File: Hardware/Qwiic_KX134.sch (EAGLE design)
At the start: 25 parts, among them J2 QWIIC_RIGHT_ANGLE, J4 QWIIC_RIGHT_ANGLE, U1 KX134

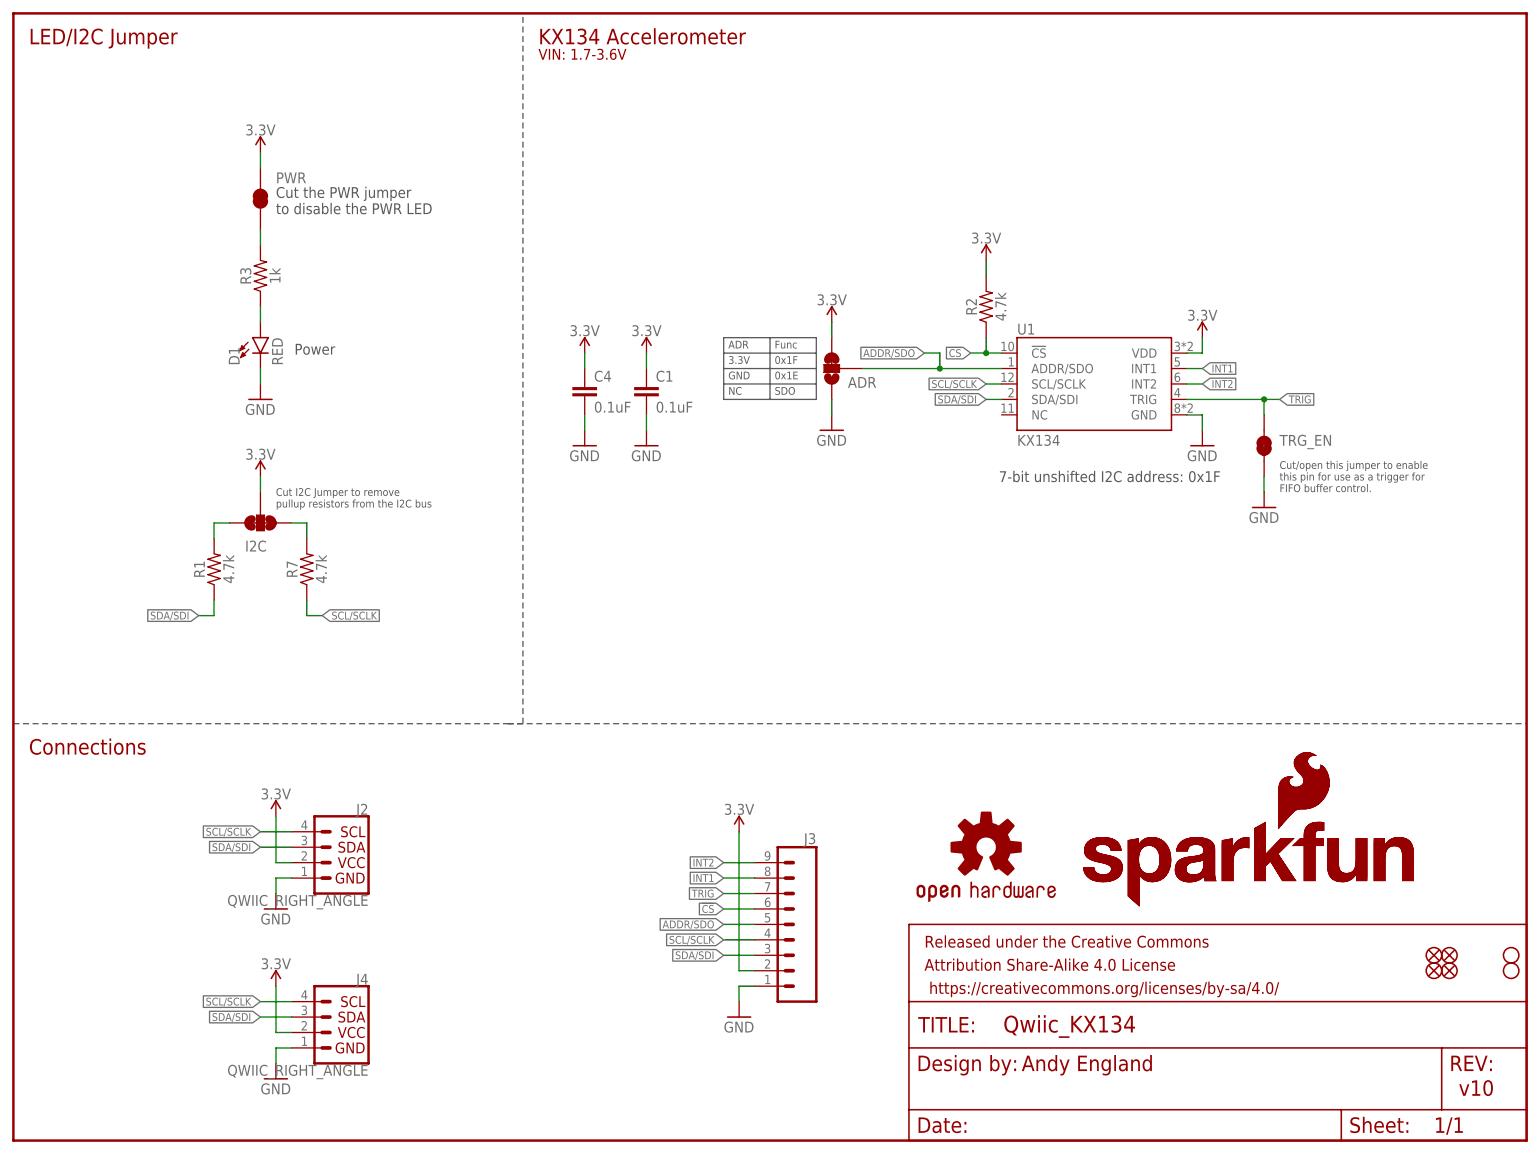
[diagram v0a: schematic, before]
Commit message: Post review/checklist changes
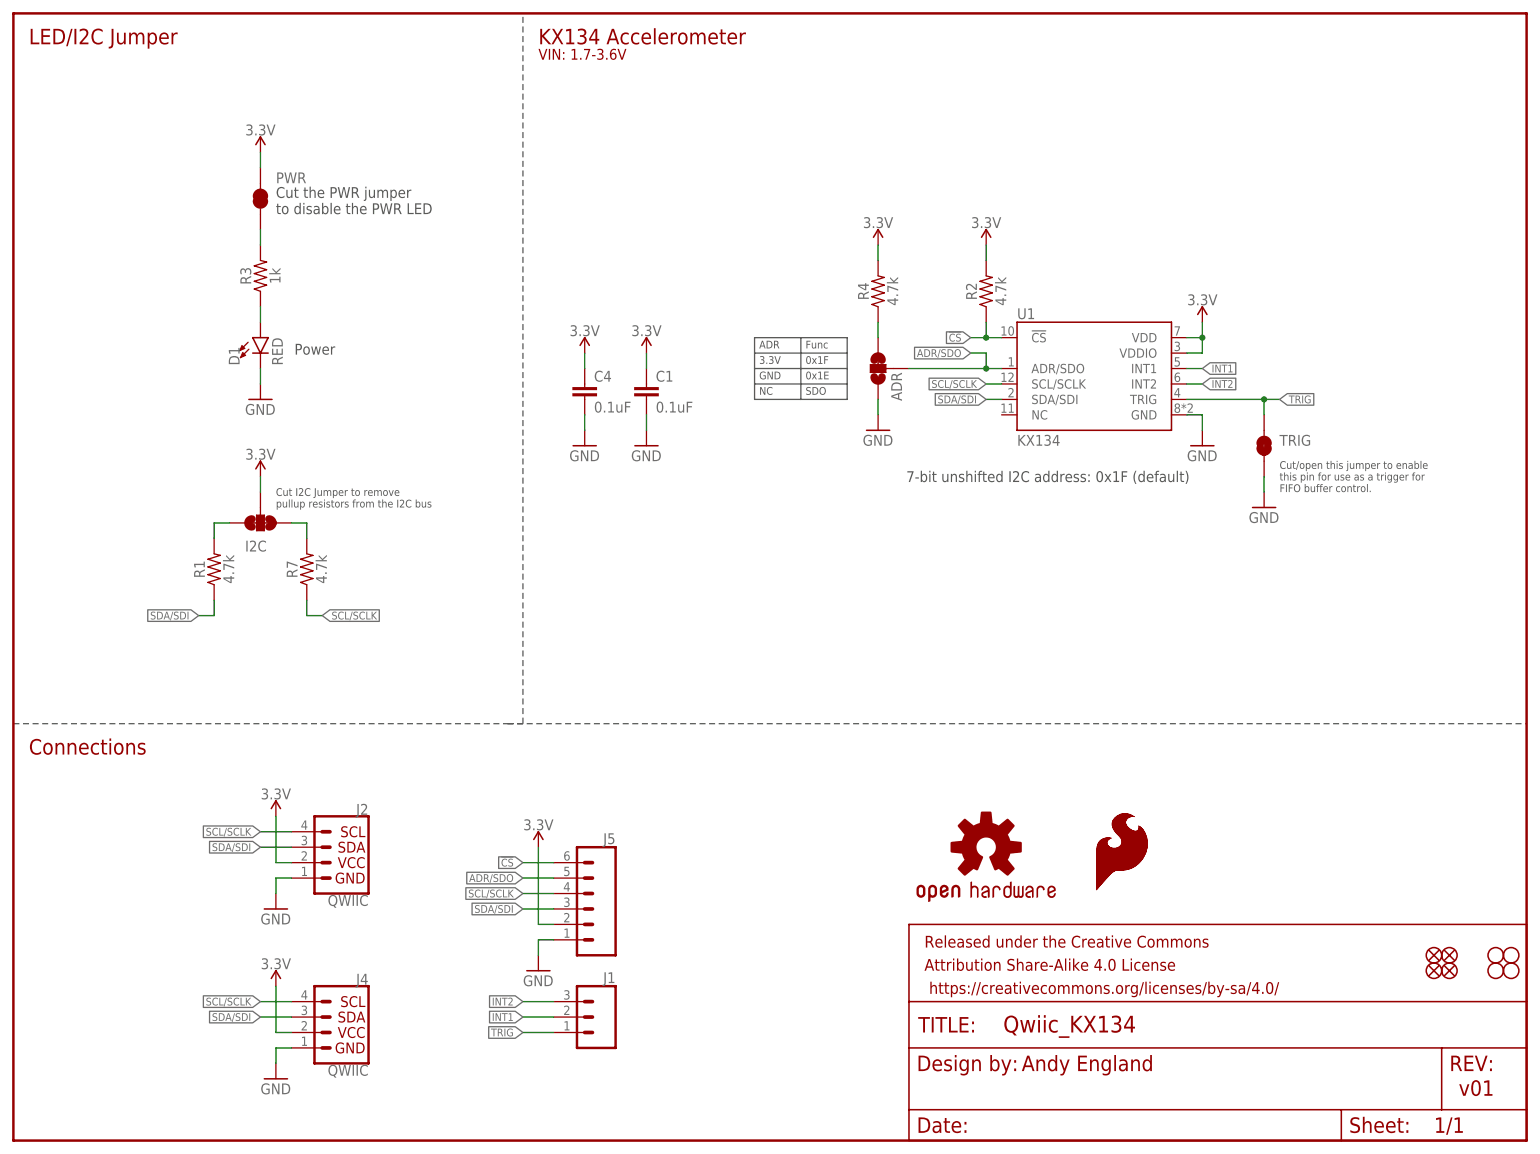
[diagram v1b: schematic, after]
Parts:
- removed J3: (no value), SparkFun-Connectors:CONN_09NO_SILK
- removed LOGO3, LOGO4: SFE_LOGO_NAME_FLAME.1_INCH, SparkFun-Aesthetics:SFE_LOGO_NAME_FLAME.1_INCH
- added J1: (no value), SparkFun-Connectors:CONN_031X03_NO_SILK
- added J5: (no value), SparkFun-Connectors:CONN_06NO_SILK_NO_POP
- added JP7, JP8: STAND-OFF, SparkFun:STAND-OFF
- added LOGO1, LOGO2: SFE_LOGO_FLAME.1_INCH, SparkFun-Aesthetics:SFE_LOGO_FLAME.1_INCH
- added R4: 4.7k, SparkFun-Resistors:4.7KOHM-0603-1/10W-1%
- J2, J4: value QWIIC_RIGHT_ANGLE -> QWIIC
- renumbered TRG_EN to TRIG
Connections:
- removed net ADDR/SDO: ADR.2, J3.5, U1.ADDR/SDO
- new net ADR/SDO: ADR.2, J5.5, U1.ADR/SDO
- new net N$5: ADR.3, R4.1
- net !CS: now also J5.6; no longer J3.6
- net 3.3V: now also J5.2, R4.2, U1.VDDIO; no longer ADR.3, J3.2
- net GND: now also J5.1; no longer J3.1
- net INT1: now also J1.2; no longer J3.8
- net INT2: now also J1.3; no longer J3.9
- net SCL/SCLK: now also J5.4; no longer J3.4
- net SDA/SDI: now also J5.3; no longer J3.3
- net TRIG: now also J1.1; no longer J3.7
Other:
- note added: "7-bit unshifted I2C address: 0x1F (default)"
- note added: "v01"
- note removed: "7-bit unshifted I2C address: 0x1F"
- note removed: "v10"
- moved on the sheet: ADR, R2

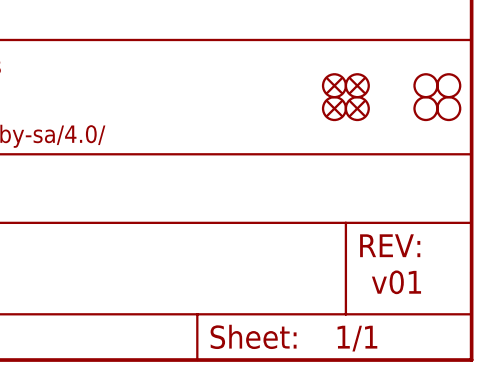
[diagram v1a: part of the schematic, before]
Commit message: updating version number and orientation for review
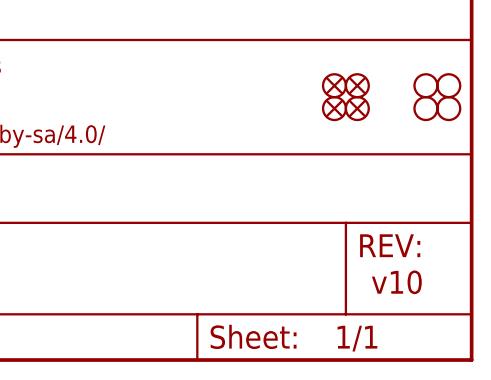
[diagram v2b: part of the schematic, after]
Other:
- note added: "v10"
- note removed: "v01"
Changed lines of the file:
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@@
 <sheet>
 <plain>
-<text x="237.744" y="7.366" size="2.54" layer="94" font="vector">v01</text>
+<text x="237.744" y="7.366" size="2.54" layer="94" font="vector">v10</text>
 <text x="170.18" y="109.22" size="1.778" layer="97" font="vector" align="center">7-bit unshifted I2C address: 0x1F (default)</text>
 <text x="46.228" y="129.286" size="1.778" layer="97" font="vector">Power</text>

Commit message: post design review, computer transfer
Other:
- note removed: "NC"
- note removed: "SDO"
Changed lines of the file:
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@@
 <wire x1="137.16" y1="129.54" x2="137.16" y2="127" width="0.1524" layer="97"/>
 <wire x1="137.16" y1="127" x2="137.16" y2="124.46" width="0.1524" layer="97"/>
-<wire x1="137.16" y1="124.46" x2="137.16" y2="121.92" width="0.1524" layer="97"/>
-<wire x1="137.16" y1="121.92" x2="129.54" y2="121.92" width="0.1524" layer="97"/>
-<wire x1="129.54" y1="121.92" x2="121.92" y2="121.92" width="0.1524" layer="97"/>
-<wire x1="121.92" y1="121.92" x2="121.92" y2="124.46" width="0.1524" layer="97"/>
 <wire x1="121.92" y1="124.46" x2="121.92" y2="127" width="0.1524" layer="97"/>
 <wire x1="121.92" y1="127" x2="121.92" y2="129.54" width="0.1524" layer="97"/>
 <wire x1="121.92" y1="129.54" x2="121.92" y2="132.08" width="0.1524" layer="97"/>
-<wire x1="129.54" y1="132.08" x2="129.54" y2="121.92" width="0.1524" layer="97"/>
+<wire x1="129.54" y1="132.08" x2="129.54" y2="124.46" width="0.1524" layer="97"/>
 <wire x1="121.92" y1="129.54" x2="137.16" y2="129.54" width="0.1524" layer="97"/>
 <wire x1="121.92" y1="127" x2="137.16" y2="127" width="0.1524" layer="97"/>
@@
 <text x="130.302" y="127.762" size="1.27" layer="97" font="vector">0x1F</text>
 <text x="130.302" y="125.222" size="1.27" layer="97" font="vector">0x1E</text>
-<text x="130.302" y="122.682" size="1.27" layer="97" font="vector">SDO</text>
 <text x="122.682" y="125.222" size="1.27" layer="97" font="vector">GND</text>
-<text x="122.682" y="122.682" size="1.27" layer="97" font="vector">NC</text>
 <wire x1="81.28" y1="68.58" x2="83.82" y2="68.58" width="0.1524" layer="97" style="longdash"/>
 <wire x1="83.82" y1="68.58" x2="83.82" y2="185.42" width="0.1524" layer="97" style="longdash"/>

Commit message: post checklist changes
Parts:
- added LOGO3: QWIIC_LOGO_4MM, SparkFun-Aesthetics:QWIIC_LOGO_4MM
- added LOGO4: SFE_LOGO_NAME_FLAME.1_INCH, SparkFun-Aesthetics:SFE_LOGO_NAME_FLAME.1_INCH
- U1: device KX134:KX134 -> SparkFun-Sensors:KX13X-KX134
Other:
- note added: "This board has two versions, KX134 and KX132"
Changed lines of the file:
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@@
 <?xml version="1.0" encoding="utf-8"?>
 <!DOCTYPE eagle SYSTEM "eagle.dtd">
-<eagle version="9.6.0">
+<eagle version="9.6.2">
 <drawing>
 <settings>
@@
 <part name="J1" library="SparkFun-Connectors" deviceset="CONN_03" device="1X03_NO_SILK"/>
 <part name="J5" library="SparkFun-Connectors" deviceset="CONN_06" device="NO_SILK_NO_POP"/>
-<part name="U1" library="KX134" deviceset="KX134" device="" value="KX134"/>
+<part name="U1" library="SparkFun-Sensors" deviceset="KX13X" device="-KX134" value="KX134"/>
 <part name="JP7" library="SparkFun" deviceset="STAND-OFF" device=""/>
 <part name="JP8" library="SparkFun" deviceset="STAND-OFF" device=""/>
 <part name="LOGO1" library="SparkFun-Aesthetics" deviceset="SFE_LOGO_FLAME" device=".1_INCH"/>
 <part name="LOGO2" library="SparkFun-Aesthetics" deviceset="SFE_LOGO_FLAME" device=".1_INCH"/>
+<part name="LOGO3" library="SparkFun-Aesthetics" deviceset="QWIIC_LOGO" device="_4MM"/>
+<part name="LOGO4" library="SparkFun-Aesthetics" deviceset="SFE_LOGO_NAME_FLAME" device=".1_INCH"/>
 </parts>
 <sheets>
@@
 <text x="2.54" y="180.34" size="2.54" layer="94" font="vector">LED/I2C Jumper</text>
 <text x="2.54" y="63.5" size="2.54" layer="94" font="vector">Connections</text>
+<text x="86.36" y="175.26" size="1.778" layer="94" font="vector">This board has two versions, KX134 and KX132</text>
 </plain>
 <instances>
@@
 <instance part="JP7" gate="G$1" x="243.84" y="27.94" smashed="yes"/>
 <instance part="JP8" gate="G$1" x="243.84" y="30.48" smashed="yes"/>
-<instance part="LOGO1" gate="G$1" x="177.8" y="40.64" smashed="yes"/>
-<instance part="LOGO2" gate="G$1" x="177.8" y="40.64" smashed="yes"/>
+<instance part="LOGO1" gate="G$1" x="220.472" y="53.086" smashed="yes"/>
+<instance part="LOGO2" gate="G$1" x="220.472" y="53.086" smashed="yes"/>
+<instance part="LOGO3" gate="G$1" x="236.22" y="40.64" smashed="yes"/>
+<instance part="LOGO4" gate="G$1" x="187.96" y="40.64" smashed="yes"/>
 </instances>
 <busses>
